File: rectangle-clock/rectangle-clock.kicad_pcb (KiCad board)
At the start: 2 copper layers, 140 x 90 mm, 41 parts, among them J1 PJ-102AH, J2 Conn_01x06, J3 Conn_01x07, SW1 Omron_B3F_SPST, SW2 Omron_B3F_SPST, SW3 Omron_B3F_SPST, SW4 Omron_B3F_SPST, U1 ATmega328-PU, U2 L7805_TO92, U3 MAX7219, U4 DS1307_DIP-8, Y1 Crystal_16MHz, Y2 Crystal_32768Hz

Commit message: initial gerber out
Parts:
- removed the J1 at (206.7, 129.5)
- added J2: Power_inlet_vertical, footprints:Wurth-694106402002, F.Cu at (188.5, 129.0)
- C3, C4: value C_22pf -> C_0805_22pf
- C6: value C_0.1uf -> C_0805_0.1uf
- DS1: renamed from DS2; value Display 2 -> LED_Display_1001
- DS2: renamed from DS1; value Display 1 -> LED_Display_1001
- R1, R3, R4: value R_10K -> R_0805_10K
- R13: value R_2.2K -> R_0805_2.2K
- U2: value L7805_TO92 -> L7805; footprint footprints:TO-92_Inline -> footprints:TO-252-2
- moved C7 20.3 mm to (208.0, 126.2), turned to 0 degrees
- moved C5 19.7 mm to (208.0, 129.5), turned to 0 degrees
- moved BT1 7.31 mm to (99.6, 92.5)
- moved U2 4.46 mm to (199.8, 128.2), turned to 180 degrees
- renumbered J3 to J1, J2 to J3, R7 to R6, R6 to R7, U4 to U1, U1 to U3, U3 to U4, Y2 to Y1, Y1 to Y2
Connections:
- C5 pad 1: Net-(C5-Pad1) -> Net-(U2-Pad1)
- U2 pad 1: VCC -> Net-(U2-Pad1)
- U2 pad 3: Net-(C5-Pad1) -> VCC
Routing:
- net GND: track 26.7 -> 131.7 mm, vias 0 -> 8
- net Net-(U2-Pad1): track 0.00 -> 39.4 mm
- net Net-(C5-Pad1): track 15.1 -> 0.00 mm
- net Net-(BT1-Pad1): track 46.8 -> 58.6 mm
- net B1: track 17.9 -> 25.9 mm
- net RESET: track 87.5 -> 95.5 mm
- net B3: track 32.1 -> 40.1 mm
- net B2: track 19.2 -> 23.8 mm
- net VCC: track 7.24 -> 3.36 mm
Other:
- board text added: "Jolly Rancher Board"

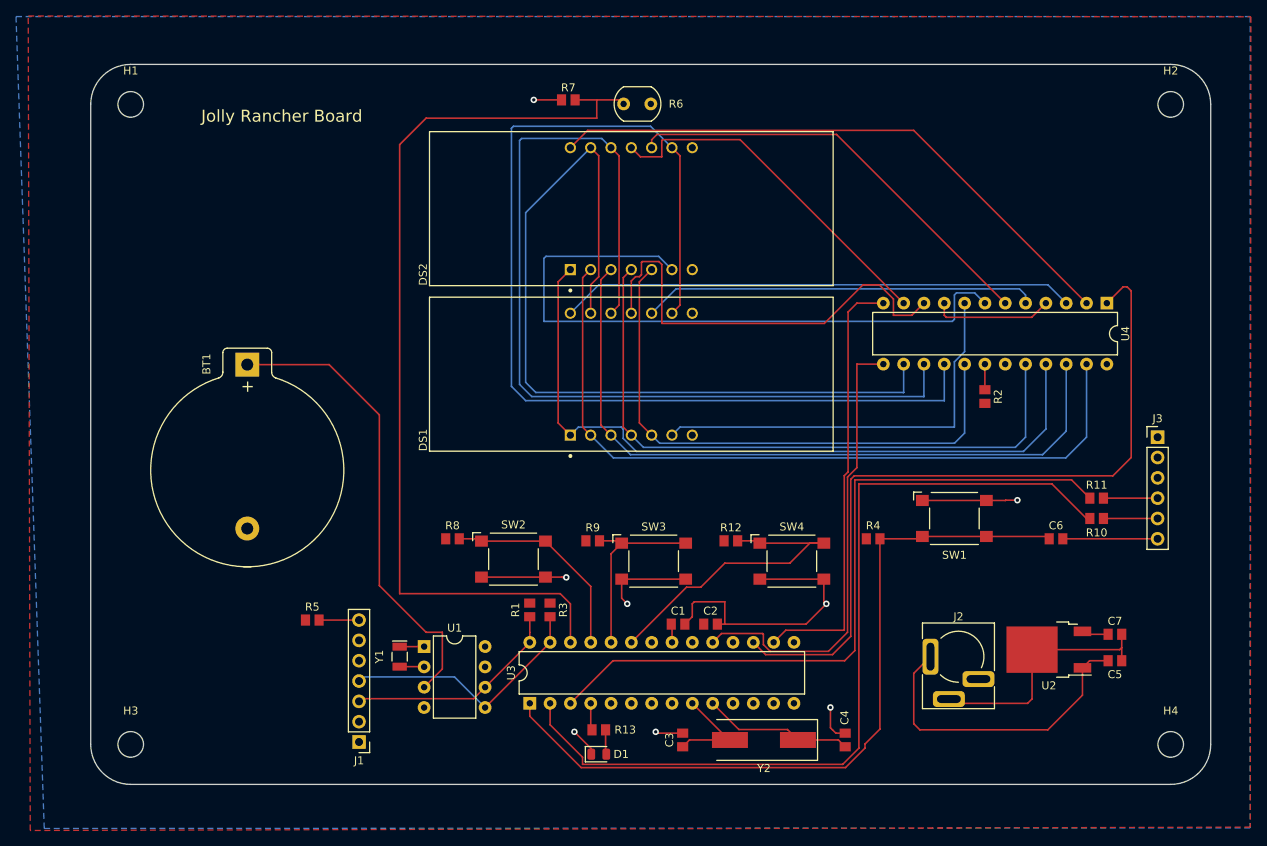
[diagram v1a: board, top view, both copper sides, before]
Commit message: Added Test points
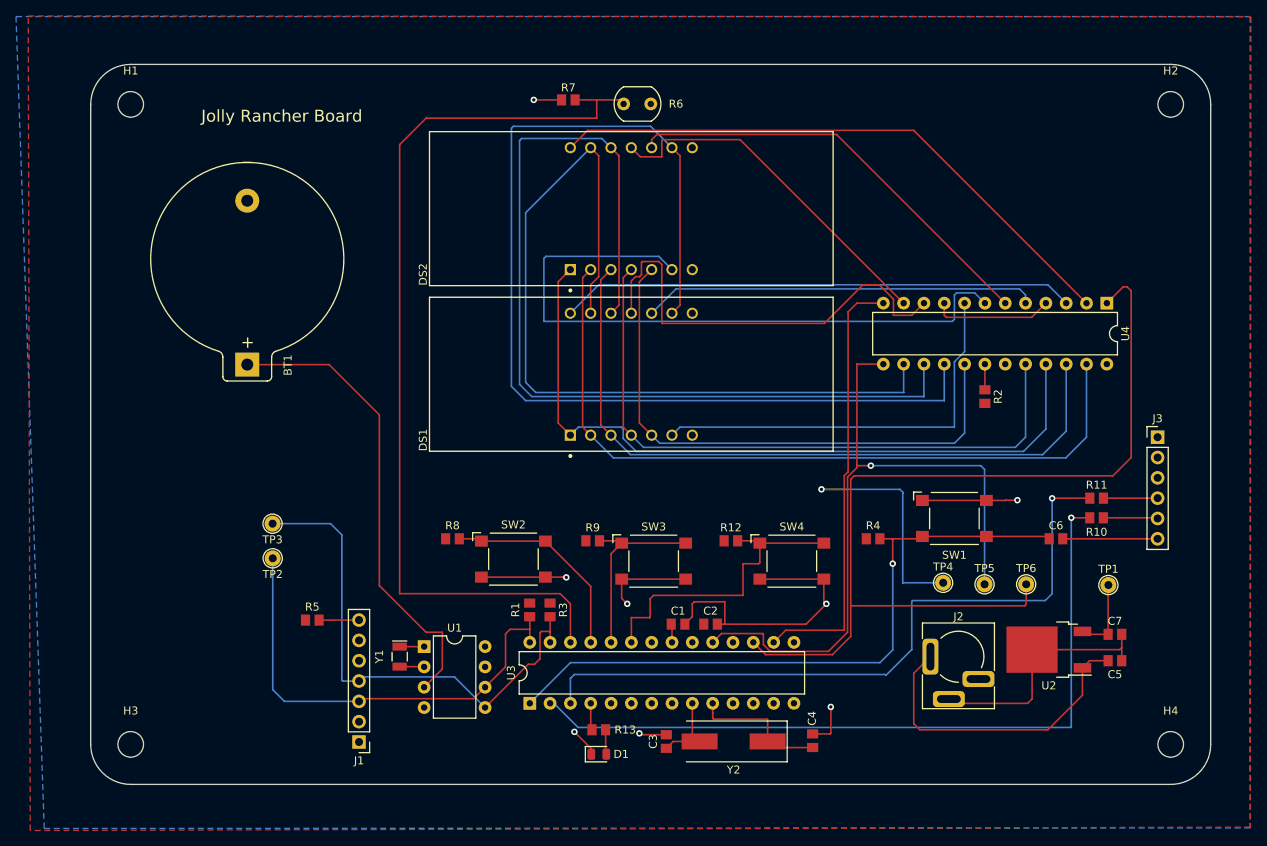
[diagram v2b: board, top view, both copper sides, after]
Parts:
- added TP1: TestPoint, footprints:TestPoint_THTPad_D2.0mm_Drill1.0mm, F.Cu at (207.2, 120.1)
- added TP2: TestPoint, footprints:TestPoint_THTPad_D2.0mm_Drill1.0mm, F.Cu at (102.8, 116.7)
- added TP3: TestPoint, footprints:TestPoint_THTPad_D2.0mm_Drill1.0mm, F.Cu at (102.7, 112.4)
- added TP4: TestPoint, footprints:TestPoint_THTPad_D2.0mm_Drill1.0mm, F.Cu at (186.6, 119.8)
- added TP5: TestPoint, footprints:TestPoint_THTPad_D2.0mm_Drill1.0mm, F.Cu at (191.7, 120.0)
- added TP6: TestPoint, footprints:TestPoint_THTPad_D2.0mm_Drill1.0mm, F.Cu at (196.9, 120.0)
- moved C4 4.07 mm to (170.2, 139.5)
- moved Y2 3.80 mm to (160.4, 139.6)
- moved C3 2.05 mm to (151.9, 139.6)
- moved R10 0.08 mm to (205.7, 111.7)
- turned BT1 to 90 degrees
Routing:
- net SDA: track 32.3 -> 64.3 mm
- net SCL: track 27.6 -> 58.5 mm
- net SCK: track 57.3 -> 87.8 mm, vias 0 -> 1
- net CS: track 54.3 -> 84.0 mm, vias 0 -> 1
- net Din: track 94.5 -> 119.0 mm
- net RXD: track 108.4 -> 94.9 mm, vias 0 -> 1
- net RESET: track 95.5 -> 83.5 mm, vias 0 -> 1
- net VCC: track 3.36 -> 9.53 mm
- net Net-(C3-Pad1): track 12.9 -> 9.66 mm
- net TXD: track 89.9 -> 88.0 mm, vias 0 -> 1
- net Net-(C4-Pad1): track 18.8 -> 17.5 mm
- net B3: track 40.1 -> 39.0 mm
- net GND: track 131.7 -> 132.7 mm

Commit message: Final gerber commit
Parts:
- added G***: LOGO, footprints:HPS_logo, F.Cu at (195.1, 71.7)
- R5: value R_0805_1K -> R_0805_10K
- moved R7 54.6 mm to (113.2, 107.2), turned to -90 degrees
- moved R6 51.4 mm to (113.2, 95.9), turned to -90 degrees
- moved TP2 14.9 mm to (94.7, 104.2), turned to -90 degrees
- moved TP3 8.78 mm to (99.3, 104.3), turned to -90 degrees
- moved R5 8.64 mm to (105.6, 116.1)
- moved J1 8.48 mm to (112.2, 131.3)
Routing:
- net PHR: track 117.4 -> 56.6 mm
- net SCL: track 58.5 -> 74.0 mm
- net DIG0: track 74.4 -> 88.3 mm
- net SDA: track 64.3 -> 76.3 mm
- net DIG2: track 54.2 -> 64.2 mm
- net DIG1: track 45.1 -> 54.3 mm
- net Net-(BT1-Pad1): track 58.6 -> 60.5 mm
- net Net-(J1-Pad7): track 4.99 -> 5.74 mm

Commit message: Final update
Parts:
- J2: moved to B.Cu
- turned J2 to 180 degrees
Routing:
- net Net-(C5-Pad1): track 39.4 -> 59.8 mm
- net GND: track 132.7 -> 129.9 mm

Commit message: Revised Board/Final Gerber out
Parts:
- added C8: C_0805_10uf, footprints:C_0805_2012Metric, F.Cu at (197.1, 96.2)
- added C9: C_0805_0.1uf, footprints:C_0805_2012Metric, F.Cu at (197.0, 99.5)
- added J4: Conn_02x03_Odd_Even, footprints:PinHeader_2x03_P2.54mm_Vertical, F.Cu at (182.9, 130.8)
- R1, R3: value R_0805_10K -> R_0805_4.7K
- R12, R8, R9: value R_0805_1K -> R_0805_10K
- R2: value R_0805_10K -> R_0805_22K
- R7: value R_0805_1K -> R_0805_100K
- moved R4 12.4 mm to (167.0, 108.3), turned to -90 degrees
- moved J2 4.72 mm to (193.2, 129.1)
- moved U2 4.72 mm to (204.5, 128.2)
- moved C5 4.72 mm to (212.7, 129.6)
- moved C7 4.72 mm to (212.7, 126.3)
- moved TP1 3.58 mm to (210.8, 120.0)
- moved R2 0.88 mm to (191.8, 97.4)
- moved R9 0.48 mm to (142.3, 114.8)
- moved R8 0.20 mm to (125.0, 114.3)
- moved R7 0.20 mm to (113.2, 107.4)
- moved R12 0.15 mm to (159.9, 114.6)
- moved R1 0.13 mm to (134.9, 123.1)
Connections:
- R13 pad 1: LED -> SCK
- U3 pad 18: unconnected-(U3-Pad18) -> MISO
- U3 pad 4: LED -> unconnected-(U3-Pad4)
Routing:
- net SCK: track 87.8 -> 162.6 mm
- net RESET: track 83.5 -> 150.9 mm, vias 1 -> 3
- net MISO: track 0.00 -> 30.4 mm
- net VCC: track 9.53 -> 26.7 mm, vias 0 -> 2
- net GND: track 129.9 -> 138.6 mm, vias 8 -> 9
- net Din: track 119.0 -> 127.1 mm
- net LED: track 3.38 -> 0.00 mm
- net Net-(R2-Pad1): track 3.21 -> 4.10 mm
- net Net-(C5-Pad1): track 59.8 -> 59.1 mm
- net B1: track 25.9 -> 26.5 mm
- net B3: track 39.0 -> 39.5 mm

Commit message: Final push? :)
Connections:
- J4 pad 1: VCC -> MISO
- J4 pad 2: Din -> VCC
- J4 pad 3: GND -> SCK
- J4 pad 4: MISO -> Din
- J4 pad 6: SCK -> GND
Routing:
- net RXD: track 94.9 -> 123.5 mm
- net VCC: track 26.7 -> 18.5 mm, vias 2 -> 0
- net SCK: track 162.6 -> 157.1 mm
- net MISO: track 30.4 -> 26.2 mm
- net Din: track 127.1 -> 130.2 mm
- net GND: track 138.6 -> 139.2 mm
